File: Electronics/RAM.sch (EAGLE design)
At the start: 16 parts, among them IC1 74LS32D, Q1 MMBTA42

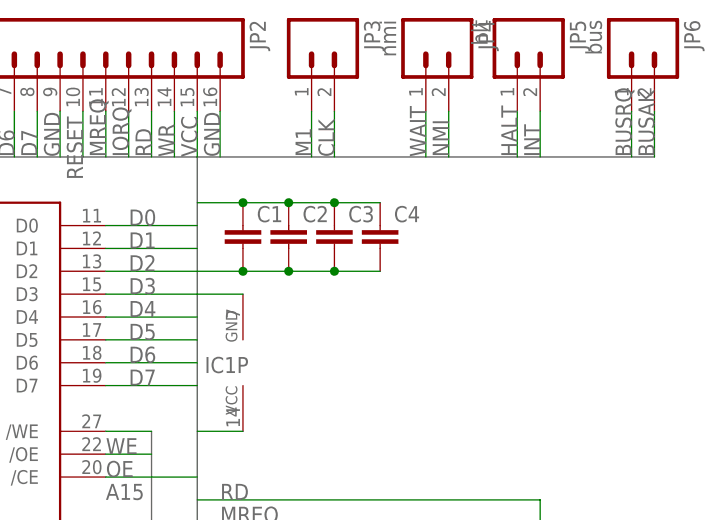
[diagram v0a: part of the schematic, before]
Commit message: Fix up caps on ram/mcu board
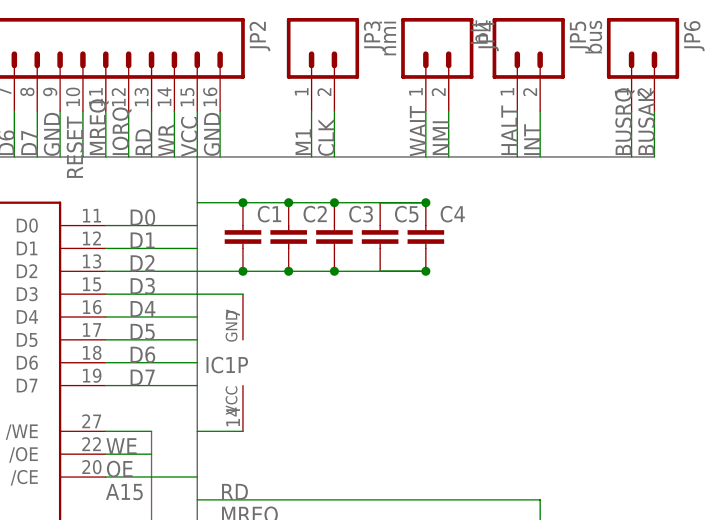
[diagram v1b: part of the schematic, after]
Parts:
- added C5: (no value), rcl:C-EUC0805
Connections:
- net GND: now also C5.2
- net VCC: now also C5.1
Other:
- moved on the sheet: C4
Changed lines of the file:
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@@
 <part name="JP5" library="SparkFun" deviceset="M02" device="PTH" value="hlt"/>
 <part name="JP6" library="SparkFun" deviceset="M02" device="PTH" value="bus"/>
+<part name="C5" library="rcl" deviceset="C-EU" device="C0805"/>
 </parts>
 <sheets>
@@
 <instance part="C2" gate="G$1" x="101.6" y="93.98"/>
 <instance part="C3" gate="G$1" x="106.68" y="93.98"/>
-<instance part="C4" gate="G$1" x="111.76" y="93.98"/>
+<instance part="C4" gate="G$1" x="116.84" y="93.98"/>
 <instance part="IC1" gate="D" x="109.22" y="22.86" rot="R180"/>
 <instance part="IC1" gate="C" x="91.44" y="22.86" rot="R180"/>
@@
 <instance part="JP5" gate="G$1" x="127" y="114.3" rot="R270"/>
 <instance part="JP6" gate="G$1" x="139.7" y="114.3" rot="R270"/>
+<instance part="C5" gate="G$1" x="111.76" y="93.98"/>
 </instances>
 <busses>
@@
 <wire x1="101.6" y1="96.52" x2="106.68" y2="96.52" width="0.1524" layer="91"/>
 <pinref part="C4" gate="G$1" pin="1"/>
-<wire x1="106.68" y1="96.52" x2="111.76" y2="96.52" width="0.1524" layer="91"/>
+<wire x1="106.68" y1="96.52" x2="116.84" y2="96.52" width="0.1524" layer="91"/>
 <junction x="101.6" y="96.52"/>
 <junction x="106.68" y="96.52"/>
+<pinref part="C5" gate="G$1" pin="1"/>
+<junction x="116.84" y="96.52"/>
+<wire x1="116.84" y1="96.52" x2="111.76" y2="96.52" width="0.1524" layer="91"/>
 </segment>
 <segment>
@@
 <wire x1="101.6" y1="88.9" x2="106.68" y2="88.9" width="0.1524" layer="91"/>
 <pinref part="C4" gate="G$1" pin="2"/>
-<wire x1="106.68" y1="88.9" x2="111.76" y2="88.9" width="0.1524" layer="91"/>
+<wire x1="106.68" y1="88.9" x2="116.84" y2="88.9" width="0.1524" layer="91"/>
 <junction x="106.68" y="88.9"/>
 <junction x="101.6" y="88.9"/>
-</segment>
-<segment>
+<pinref part="C5" gate="G$1" pin="2"/>
+<junction x="116.84" y="88.9"/>
+<wire x1="116.84" y1="88.9" x2="111.76" y2="88.9" width="0.1524" layer="91"/>
+</segment>
+<segment>
